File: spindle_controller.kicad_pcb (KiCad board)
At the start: 2 copper layers, 178.5 x 120.5 mm, 57 parts, among them J1 VAC 230V, J2 AUX/CONTROL, J3 ICP, J4 Load output, J5 CONN_01X03, J6 CONN_01X03, Q1 2N3904, SW1 Rotary_Encoder_Switch, T1 230 - 6VAC (Spitznagel SPK 01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, U1 LM7805CT, U2 ATMEGA328P-PU, U3 PC817, U4 MOC3020M, U5 TCRT5000, Y1 16MHz

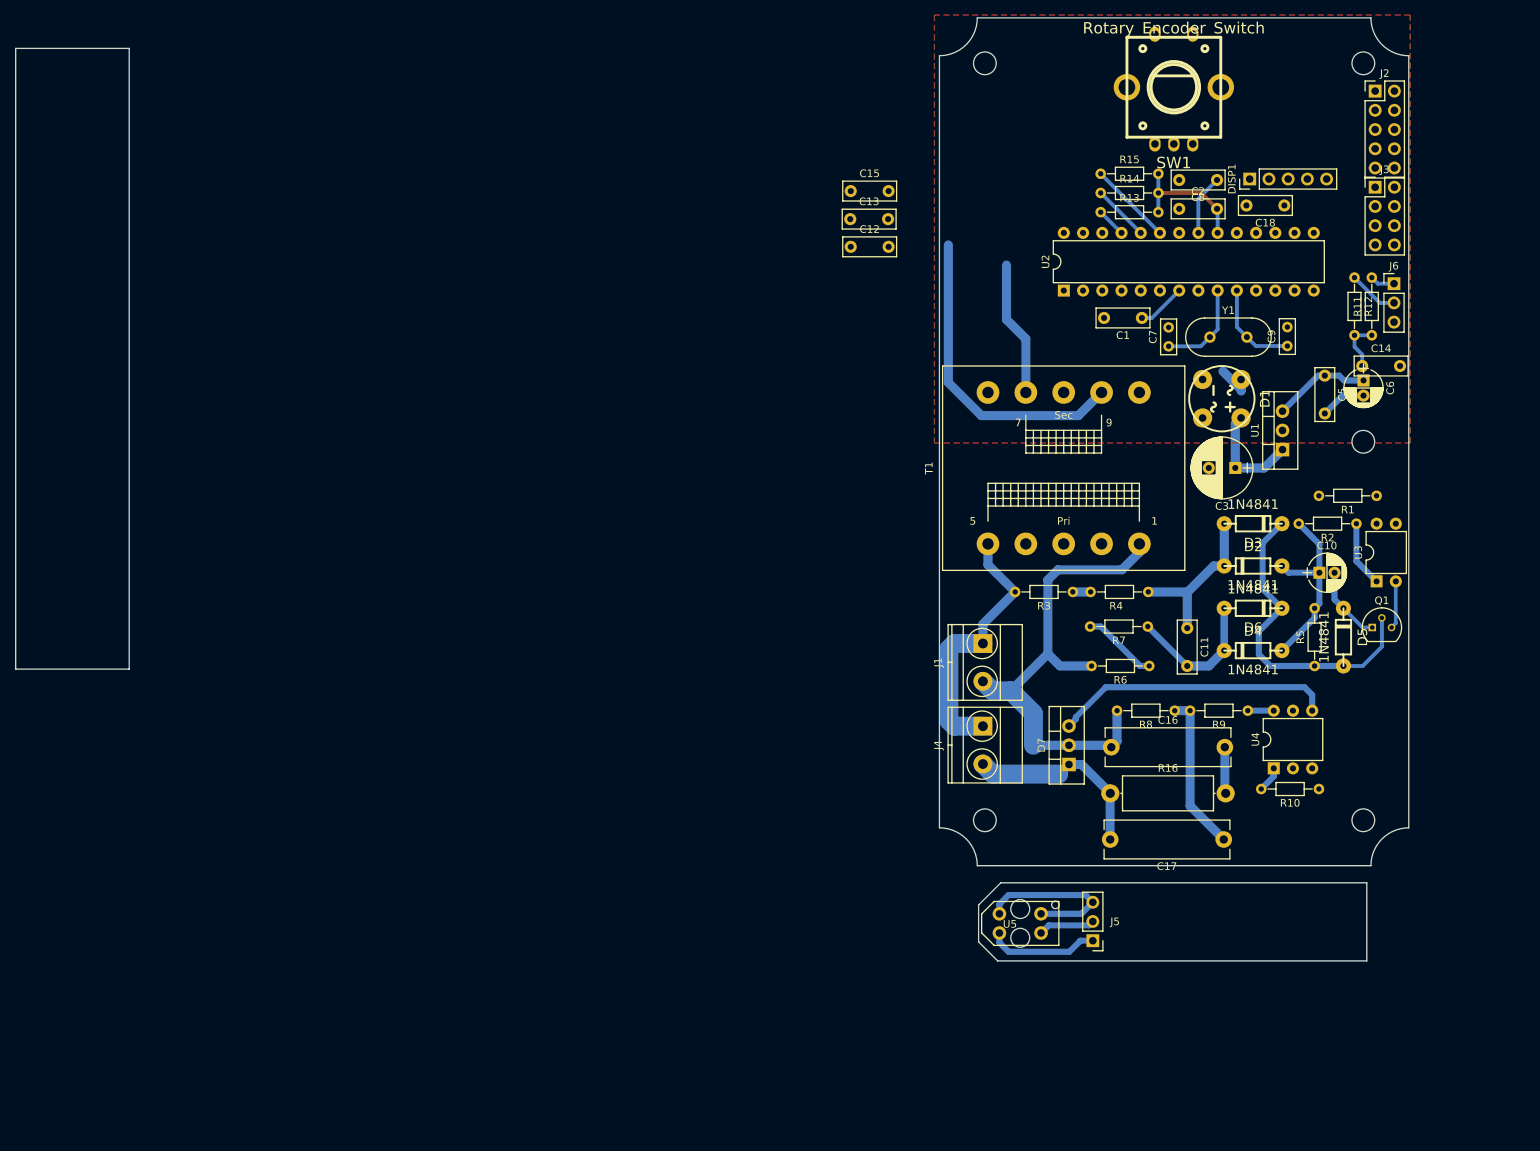
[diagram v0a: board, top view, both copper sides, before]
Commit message: Add shuffled AC cord entry, ziplock holes, 1117 regulator alternative, shuffled linear supply
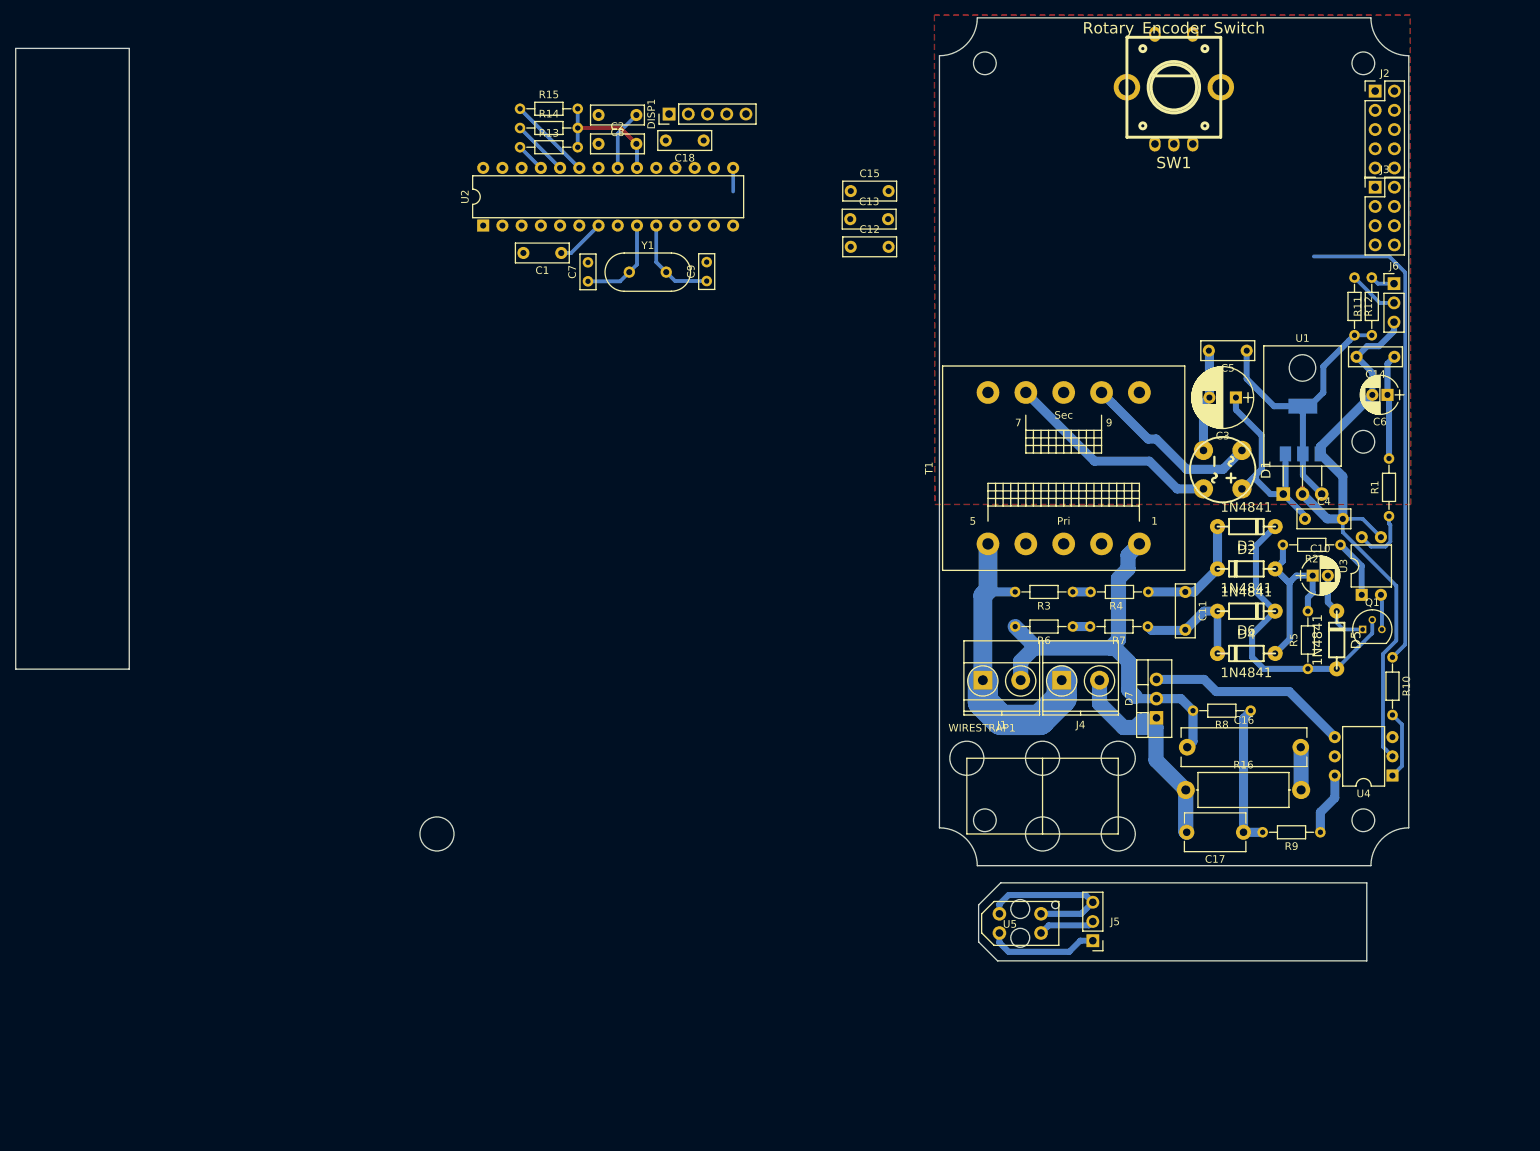
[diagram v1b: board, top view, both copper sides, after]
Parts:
- added C4: 10n, Capacitors_ThroughHole:C_Rect_L7.0mm_W2.5mm_P5.00mm, F.Cu at (118.7, 80.6)
- added U6: AP111750, TO_SOT_Packages_SMD:SOT-223, B.Cu at (118.5, 68.9)
- added WIRESTRAP1: 2x Ziplock wire strap, iotta_footprints:WireStrap_2X, F.Cu at (84.1, 112.3)
- C17: footprint Capacitors_ThroughHole:C_Rect_L16.5mm_W5.0mm_P15.00mm_MKT -> Capacitors_ThroughHole:C_Disc_D8.0mm_W5.0mm_P7.50mm
- U1: footprint TO_SOT_Packages_THT:TO-220_Vertical -> TO_SOT_Packages_THT:TO-220_Horizontal
- moved C1 77.2 mm to (20.5, 45.5)
- moved C18 77.2 mm to (39.3, 30.7)
- moved C2 77.2 mm to (25.4, 31.1)
- moved C7 77.2 mm to (24.0, 49.3)
- moved C8 77.2 mm to (30.4, 27.3)
- moved C9 77.2 mm to (39.7, 49.2)
- moved DISP1 77.2 mm to (34.7, 27.2)
- moved R13 77.2 mm to (15.0, 31.5)
- moved R14 77.2 mm to (15.0, 29.0)
- moved R15 77.2 mm to (15.0, 26.5)
- moved U2 77.2 mm to (10.2, 41.9)
- moved Y1 77.2 mm to (29.5, 48.0)
- moved R10 19.9 mm to (130.3, 98.9), turned to 270 degrees
- moved R9 18.7 mm to (120.8, 122.0)
- moved U4 15.7 mm to (130.3, 114.6), turned to 180 degrees
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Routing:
- net GND: track 6.09 -> 96.5 mm
- net /TRIAC_DRIVE: track 0.00 -> 67.6 mm
- net VCC: track 43.0 -> 77.7 mm
- net Net-(D1-Pad2): track 41.5 -> 23.8 mm
- net Net-(C3-Pad1): track 14.4 -> 29.5 mm
- net Net-(D1-Pad3): track 17.9 -> 28.7 mm
- net Net-(D7-Pad3): track 36.9 -> 26.7 mm
- net Net-(C17-Pad2): track 25.6 -> 33.7 mm
- net /ZCROSS_PULSE: track 0.00 -> 8.02 mm
- net Net-(R6-Pad1): track 9.97 -> 2.29 mm
- net Net-(C11-Pad1): track 21.8 -> 16.0 mm
- net Net-(R10-Pad2): track 3.41 -> 9.04 mm
- net /VAC_N: track 35.5 -> 40.6 mm
- net Net-(R9-Pad1): track 3.43 -> 8.28 mm
- net (no net): track 3.60 -> 0.00 mm
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
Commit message: Finish routing. Need to draw break-off slots.
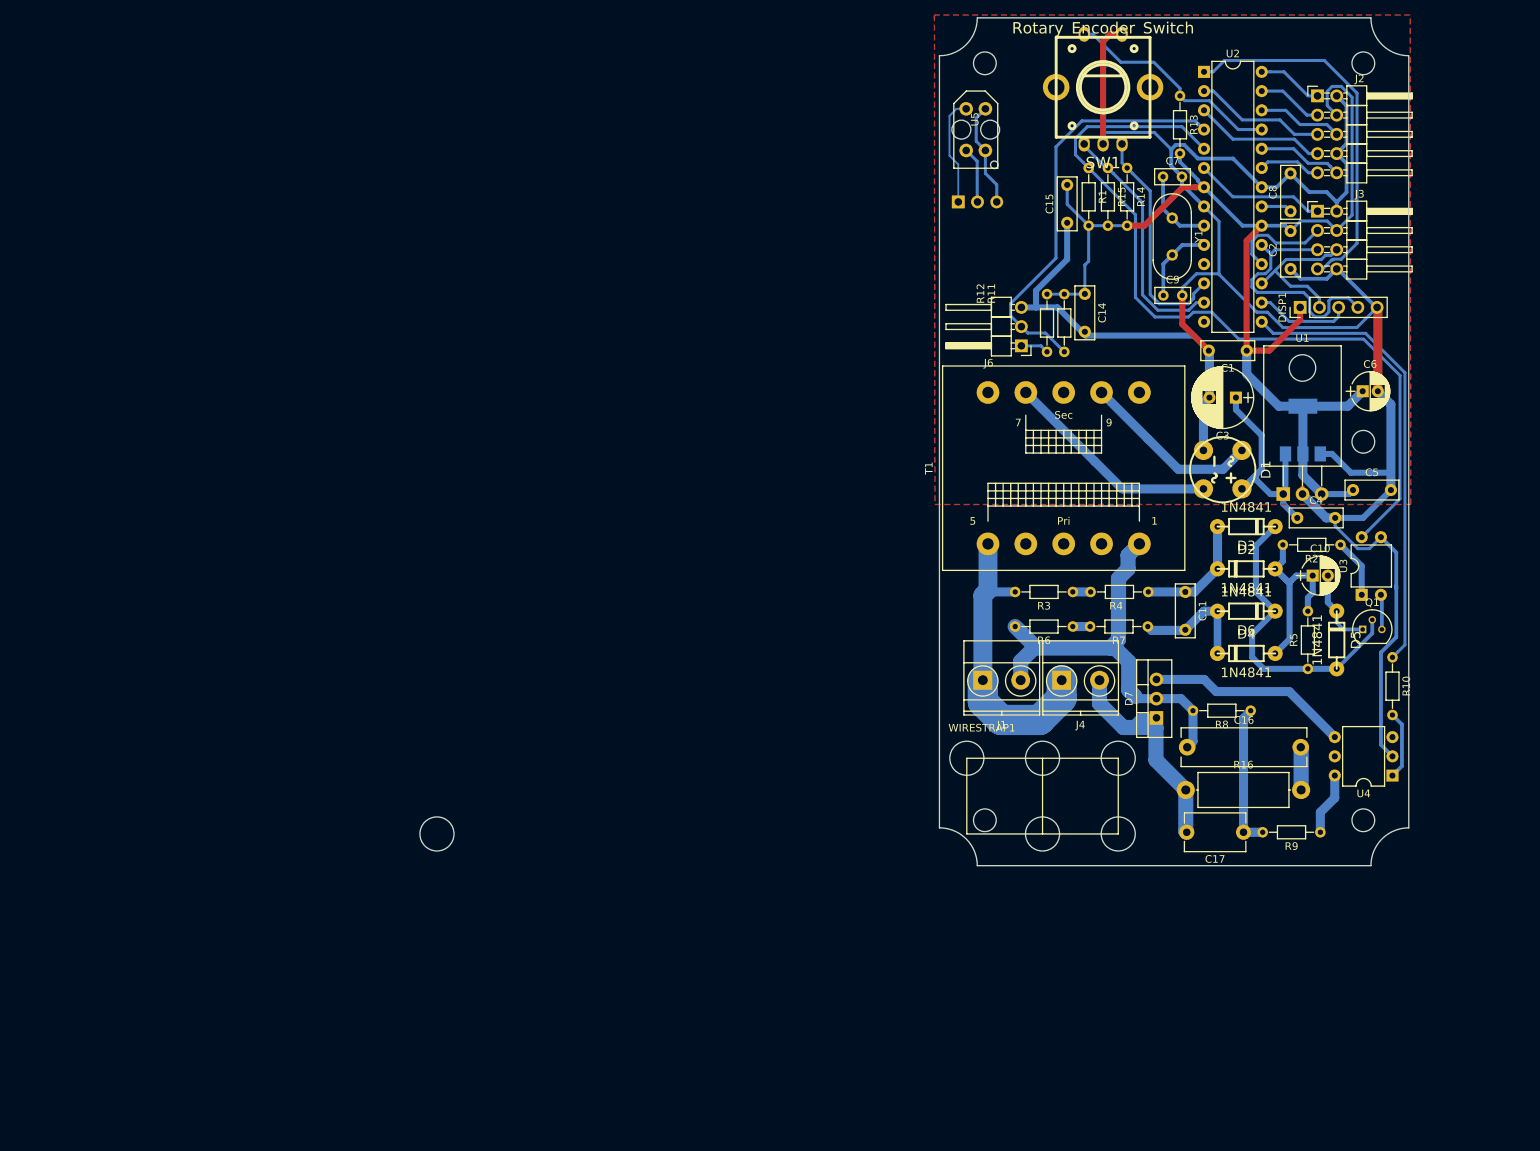
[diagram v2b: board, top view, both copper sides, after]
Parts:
- removed C12, C13, C18: 100n, Capacitors_ThroughHole:C_Rect_L7.0mm_W2.5mm_P5.00mm
- C4: value 10n -> 470n
- C5: value 10n -> 100n
- C7, C9: value 33p -> 27p
- J2: footprint Pin_Headers:Pin_Header_Straight_2x05_Pitch2.54mm -> Pin_Headers:Pin_Header_Angled_2x05_Pitch2.54mm
- J3: footprint Pin_Headers:Pin_Header_Straight_2x04_Pitch2.54mm -> Pin_Headers:Pin_Header_Angled_2x04_Pitch2.54mm
- J5: footprint Pin_Headers:Pin_Header_Straight_1x03_Pitch2.54mm -> Pin_Headers:Pin_Header_Angled_1x03_Pitch2.54mm; moved to B.Cu
- J6: footprint Pin_Headers:Pin_Header_Straight_1x03_Pitch2.54mm -> Pin_Headers:Pin_Header_Angled_1x03_Pitch2.54mm
- U1: value LM7805CT -> LM2940CT-5.0
- U6: value AP111750 -> LT1117-5
- moved U5 105.0 mm to (75.3, 29.2), turned to 90 degrees
- moved J5 99.2 mm to (72.9, 38.8), turned to 270 degrees
- moved U2 97.4 mm to (105.4, 21.6), turned to 0 degrees
- moved C2 92.9 mm to (116.8, 47.6), turned to 90 degrees
- moved C1 91.5 mm to (111.0, 58.4)
- moved R13 87.4 mm to (102.2, 24.8), turned to 270 degrees
- moved C8 87.4 mm to (116.8, 40.0), turned to 90 degrees
- moved DISP1 87.2 mm to (118.1, 52.7)
- moved R14 80.4 mm to (95.2, 34.3), turned to 270 degrees
- moved R15 78.1 mm to (92.7, 34.3), turned to 270 degrees
- moved C7 77.2 mm to (100.0, 35.4), turned to 0 degrees
- moved Y1 72.1 mm to (101.2, 40.9), turned to 270 degrees
- moved R1 60.7 mm to (90.2, 34.3), turned to 270 degrees
- moved C9 60.4 mm to (100.0, 51.1), turned to 0 degrees
- moved J6 49.9 mm to (81.3, 57.8), turned to 180 degrees
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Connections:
- DISP1 pad 1: Net-(C18-Pad2) -> VCC
- U2 pad 12: /PD6 -> /RENC_B
- U2 pad 13: /PD7 -> /RENC_A
- U2 pad 23: /RENC_A -> /PD6
- U2 pad 24: /RENC_B -> /PD7
- U2 pad 4: /ZCROSS_PULSE -> /ROT_PULSE
- U2 pad 5: /ROT_PULSE -> /ZCROSS_PULSE
- U2 pad 6: Net-(U2-Pad6) -> /DBG
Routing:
- net GND: track 96.5 -> 298.5 mm
- net /ZCROSS_PULSE: track 8.02 -> 106.3 mm
- net VCC: track 77.7 -> 158.6 mm
- net /RST: track 0.00 -> 49.1 mm
- net /ROT_PULSE: track 6.61 -> 55.3 mm
- net /SCK: track 0.00 -> 33.1 mm
- net /SW1: track 3.88 -> 29.2 mm
- net /RENC_B: track 7.47 -> 30.5 mm
- net /RENC_A: track 11.1 -> 32.6 mm
- net /MOSI: track 0.00 -> 20.3 mm
- net /DBG: track 0.00 -> 17.9 mm
- net /RX: track 0.00 -> 17.4 mm
- net /TX: track 0.00 -> 17.4 mm
- net /MISO: track 0.00 -> 13.7 mm
- net /SEG_CS: track 0.00 -> 12.7 mm
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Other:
- board size 178.5 x 120.5 mm -> 62 x 112 mm
- net class VAC: clearance 2 -> 1.5; trace_width 2 -> 1.2

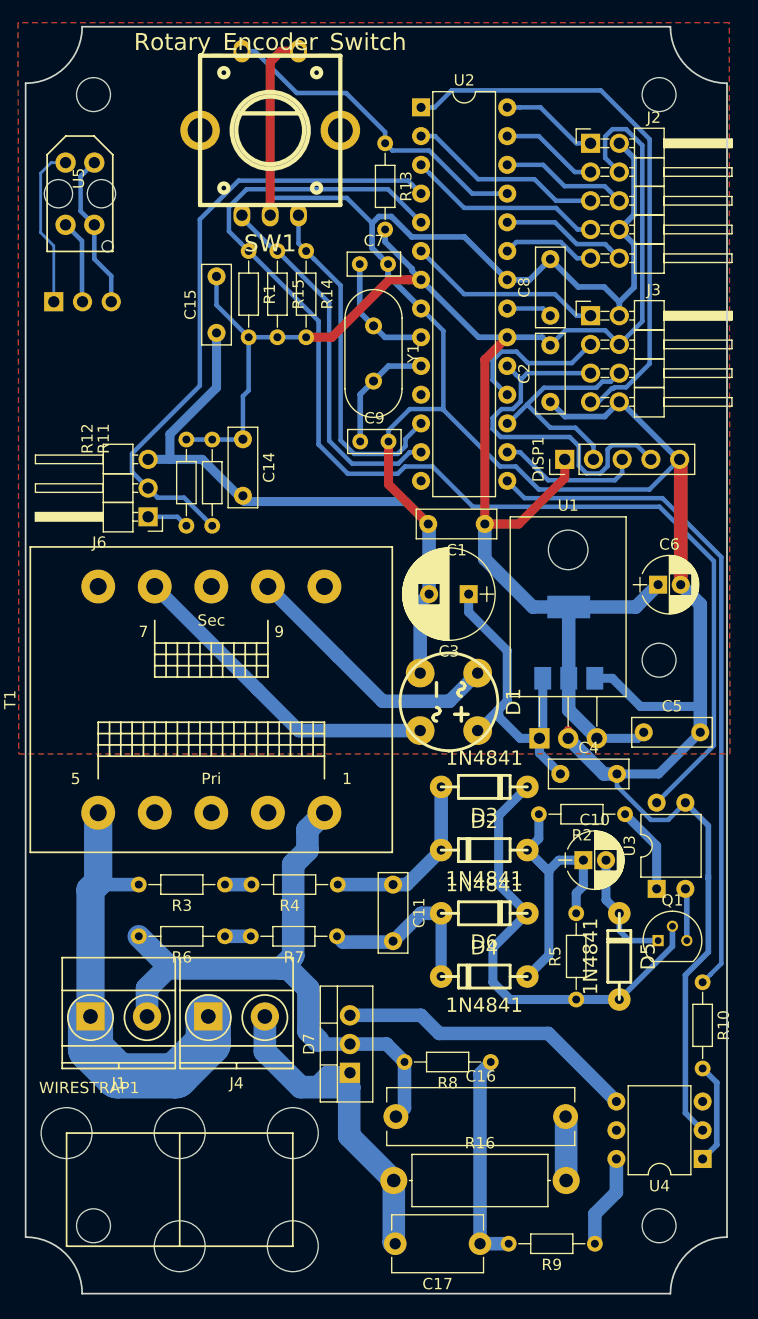
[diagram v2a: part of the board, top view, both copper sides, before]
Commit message: Add jumper wires for single sided PCB's
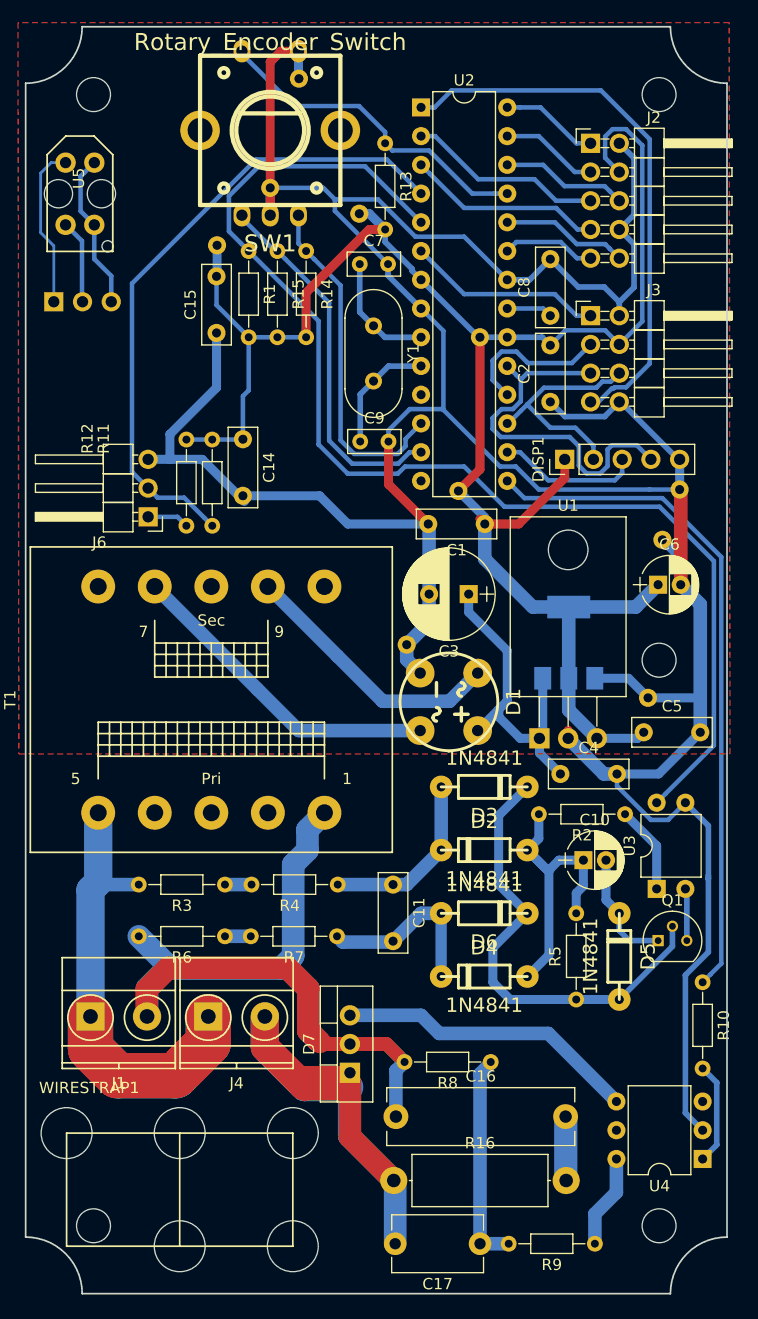
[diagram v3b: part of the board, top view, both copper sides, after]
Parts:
- added J7: GND_JUMPER, iotta_footprints:JUMPER_PIN, F.Cu at (104.1, 69.1)
- added J7: GND_JUMPER, iotta_footprints:JUMPER_PIN, F.Cu at (125.5, 73.8)
- added J7: GND_JUMPER, iotta_footprints:JUMPER_PIN, F.Cu at (94.6, 19.1)
- added J7: GND_JUMPER, iotta_footprints:JUMPER_PIN, F.Cu at (126.7, 59.8)
- added J7: GND_JUMPER, iotta_footprints:JUMPER_PIN, F.Cu at (128.3, 55.4)
- added J7: GND_JUMPER, iotta_footprints:JUMPER_PIN, F.Cu at (92.1, 28.7)
- added J8: VCC_JUMPER, iotta_footprints:JUMPER_PIN, F.Cu at (108.7, 55.5)
- added J8: VCC_JUMPER, iotta_footprints:JUMPER_PIN, F.Cu at (87.4, 33.8)
- added J8: VCC_JUMPER, iotta_footprints:JUMPER_PIN, F.Cu at (99.9, 31.0)
- added J8: VCC_JUMPER, iotta_footprints:JUMPER_PIN, F.Cu at (110.6, 41.9)
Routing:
- net Net-(C17-Pad2): track 33.7 -> 80.3 mm
- net /VAC_L: track 64.6 -> 95.5 mm
- net /VAC_N: track 40.6 -> 61.5 mm
- net GND: track 298.5 -> 307.7 mm
- net VCC: track 158.6 -> 166.7 mm
- net Net-(C16-Pad2): track 5.67 -> 11.3 mm
- net /ZCROSS_PULSE: track 106.3 -> 108.6 mm
- net /ROT_PULSE: track 55.3 -> 57.1 mm
